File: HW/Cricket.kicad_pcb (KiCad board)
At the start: 2 copper layers, 17 parts, among them P1 CONN_01X02, P2 CONN_01X01, P3 CONN_01X04, Q1 Si2312CDS, Q2 Q_NPN_BEC, SW1 SPDT_SLIDE, U1 MSP430G2230ID

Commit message: layout finished, gerbers etc.
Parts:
- D1: footprint nightmechanic_pcb:SMD_MiniLED -> SMD_MiniLED
- moved C1 48.8 mm to (122.3, 95.7)
- moved P1 48.8 mm to (126.2, 82.4)
- moved BAT1 48.8 mm to (102.6, 87.5)
- moved D1 48.8 mm to (124.1, 76.9)
- moved P3 48.8 mm to (111.6, 76.9)
- moved Q1 48.8 mm to (107.1, 81.2)
- moved Q2 48.8 mm to (125.0, 87.6)
- moved R1 48.8 mm to (120.4, 88.0)
- moved SW1 48.8 mm to (102.6, 87.5)
- moved C2 48.7 mm to (117.3, 81.8)
- moved R4 48.7 mm to (121.6, 81.8)
- moved R5 48.7 mm to (113.5, 81.8)
- moved U1 48.7 mm to (110.7, 89.1)
- moved R2 48.6 mm to (107.8, 97.2)
- moved R3 48.6 mm to (111.8, 97.2)
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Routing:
- net GND: track 25.7 -> 27.7 mm, vias 10 -> 11
- net Net-(P2-Pad1): track 4.69 -> 3.62 mm
- net /SBWTDIO: track 13.7 -> 14.6 mm
- net Net-(Q2-Pad1): track 13.4 -> 14.2 mm
- net Net-(R4-Pad1): track 11.3 -> 10.8 mm
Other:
- board outline added: 29 x 25 mm
- net class Bat-: via_dia 0.6 -> 0.8; via_drill 0.4 -> 0.55
- net class Default: via_dia 0.6 -> 0.8; via_drill 0.4 -> 0.55
- board text added: "Cricket V1.0 ©Nightmechanic 2016"
- board text added: "Vcc TCK TDIO GND"

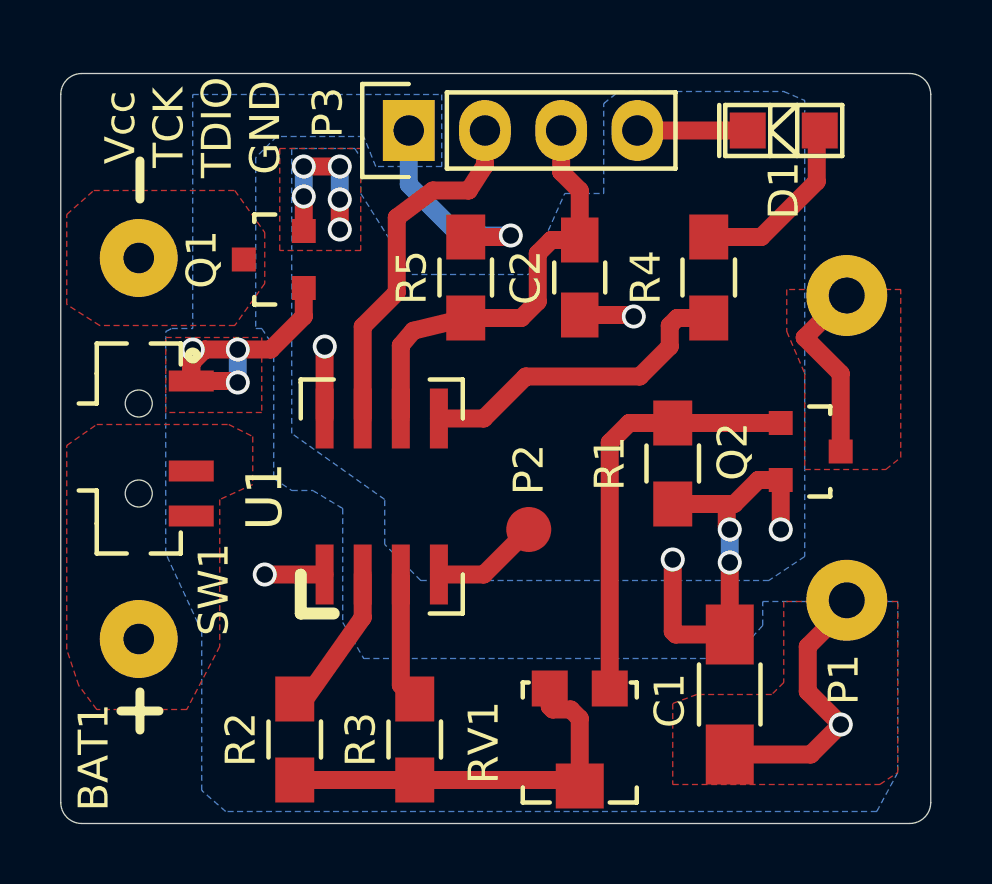
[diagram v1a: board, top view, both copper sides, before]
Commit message: reduce solder make expansion
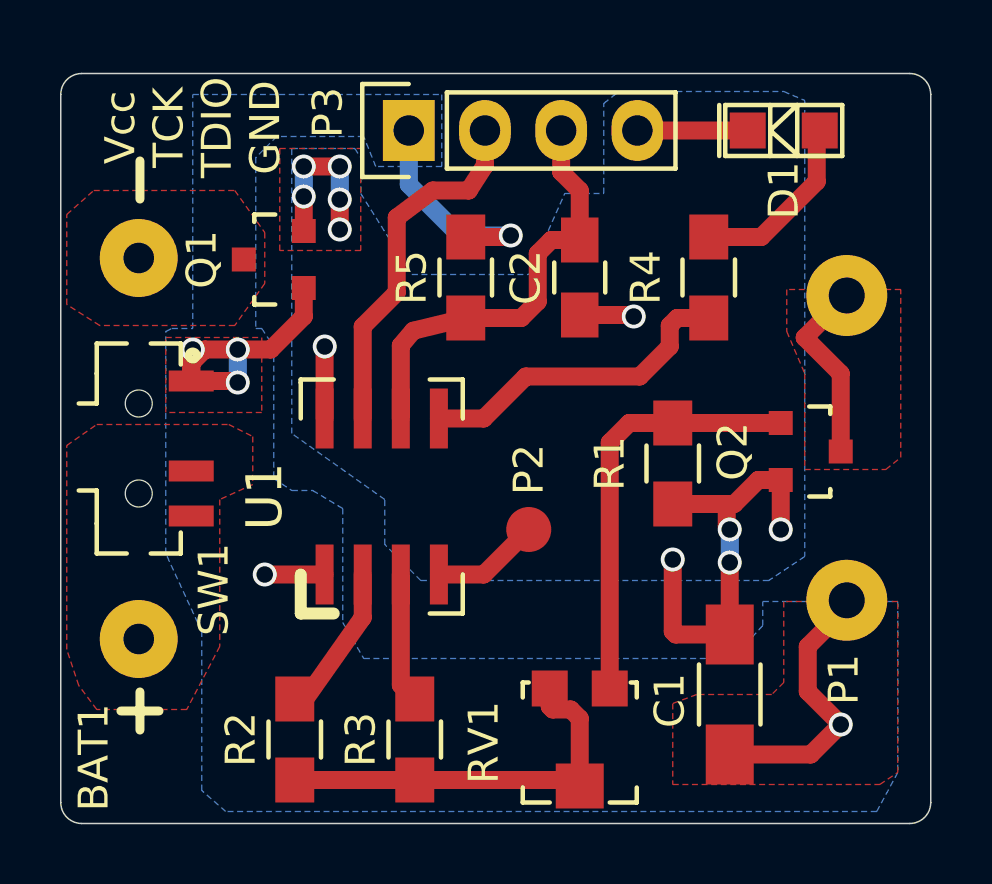
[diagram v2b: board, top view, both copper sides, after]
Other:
- rule pad_to_mask_clearance: 0.2 -> 0.05
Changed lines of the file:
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@@
   (page A4)
   (layers
-    (0 F.Cu signal)
-    (31 B.Cu signal)
+    (0 F.Cu signal hide)
+    (31 B.Cu signal hide)
     (32 B.Adhes user)
     (33 F.Adhes user)
@@
     (trace_min 0.2)
     (segment_width 0.2)
-    (edge_width 0.001)
+    (edge_width 0.05)
     (via_size 0.8)
     (via_drill 0.55)
@@
     (pcb_text_width 0.3)
     (pcb_text_size 1.5 1.5)
-    (mod_edge_width 0.15)
+    (mod_edge_width 0.05)
     (mod_text_size 1 1)
     (mod_text_width 0.15)
     (pad_size 1.524 1.524)
     (pad_drill 0.762)
-    (pad_to_mask_clearance 0.2)
+    (pad_to_mask_clearance 0.05)
     (aux_axis_origin 0 0)
     (grid_origin 100 100)
@@
     (effects (font (size 1 1) (thickness 0.15)))
   )
-  (gr_arc (start 128.3 99.3) (end 129 99.3) (angle 90) (layer Edge.Cuts) (width 0.001))
-  (gr_arc (start 128.3 75.7) (end 128.3 75) (angle 90) (layer Edge.Cuts) (width 0.001))
-  (gr_arc (start 100.7 75.7) (end 100 75.7) (angle 90) (layer Edge.Cuts) (width 0.001))
-  (gr_arc (start 100.7 99.3) (end 100.7 100) (angle 90) (layer Edge.Cuts) (width 0.001))
-  (gr_line (start 128.3 100) (end 100.7 100) (angle 90) (layer Edge.Cuts) (width 0.001))
-  (gr_line (start 129 75.7) (end 129 99.3) (angle 90) (layer Edge.Cuts) (width 0.001))
-  (gr_line (start 100.7 75) (end 128.3 75) (angle 90) (layer Edge.Cuts) (width 0.001))
-  (gr_line (start 100 99.3) (end 100 75.7) (angle 90) (layer Edge.Cuts) (width 0.001))
+  (gr_arc (start 128.3 99.3) (end 129 99.3) (angle 90) (layer Edge.Cuts) (width 0.05))
+  (gr_arc (start 128.3 75.7) (end 128.3 75) (angle 90) (layer Edge.Cuts) (width 0.05))
+  (gr_arc (start 100.7 75.7) (end 100 75.7) (angle 90) (layer Edge.Cuts) (width 0.05))
+  (gr_arc (start 100.7 99.3) (end 100.7 100) (angle 90) (layer Edge.Cuts) (width 0.05))
+  (gr_line (start 128.3 100) (end 100.7 100) (angle 90) (layer Edge.Cuts) (width 0.05))
+  (gr_line (start 129 75.7) (end 129 99.3) (angle 90) (layer Edge.Cuts) (width 0.05))
+  (gr_line (start 100.7 75) (end 128.3 75) (angle 90) (layer Edge.Cuts) (width 0.05))
+  (gr_line (start 100 99.3) (end 100 75.7) (angle 90) (layer Edge.Cuts) (width 0.05))
   (segment (start 113.5 80.45) (end 114.95 80.45) (width 0.6) (layer F.Cu) (net 1))
   (segment (start 111.6 78.7) (end 111.6 76.9) (width 0.6) (layer B.Cu) (net 1))
@@
   (via (at 105.9 85.3) (size 0.8) (drill 0.55) (layers F.Cu B.Cu) (net 1))
   (segment (start 105.85 85.25) (end 105.9 85.3) (width 0.6) (layer F.Cu) (net 1))
-  (segment (start 123.99924 88.55) (end 123.99924 90.19924) (width 0.6) (layer F.Cu) (net 2) (status 400000))
+  (segment (start 123.99924 88.55) (end 123.99924 90.19924) (width 0.6) (layer F.Cu) (net 2))
   (via (at 124 90.2) (size 0.8) (drill 0.55) (layers F.Cu B.Cu) (net 2))
   (segment (start 123.99924 90.19924) (end 124 90.2) (width 0.6) (layer F.Cu) (net 2))
